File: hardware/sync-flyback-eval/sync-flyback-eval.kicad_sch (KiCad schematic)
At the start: 89 parts, among them J1 RJ45_LED_Shielded, Q1 SiR422DP, Q2 Si7898DP, Q3 MMDT3906, T1 PoE_Transformer, T2 Pulse_Transformer, U1 TPS23754PWPR, U2 TCMT1107

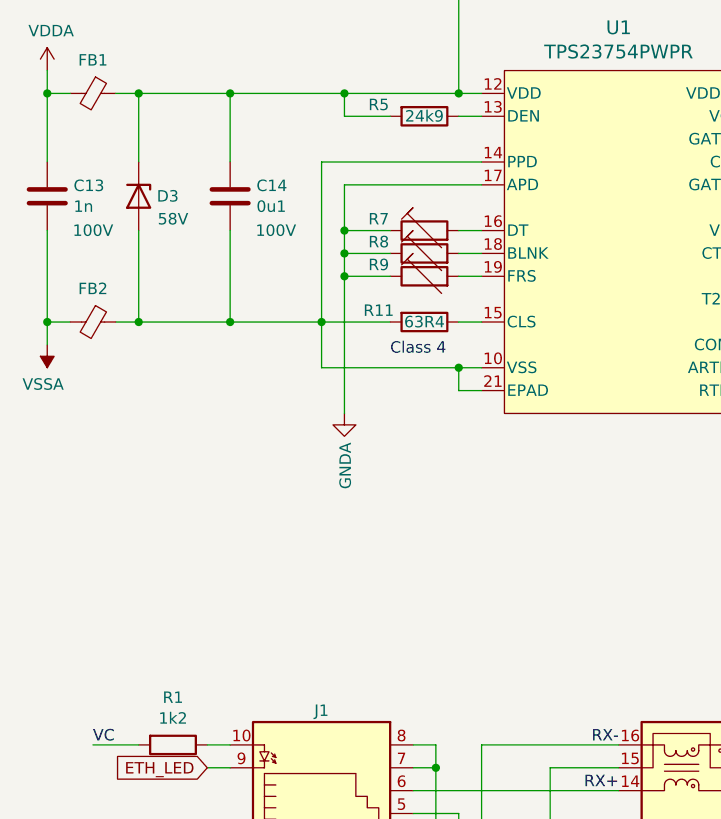
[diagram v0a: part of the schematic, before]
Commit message: flyback: use trimpots instead of trimmable resistors
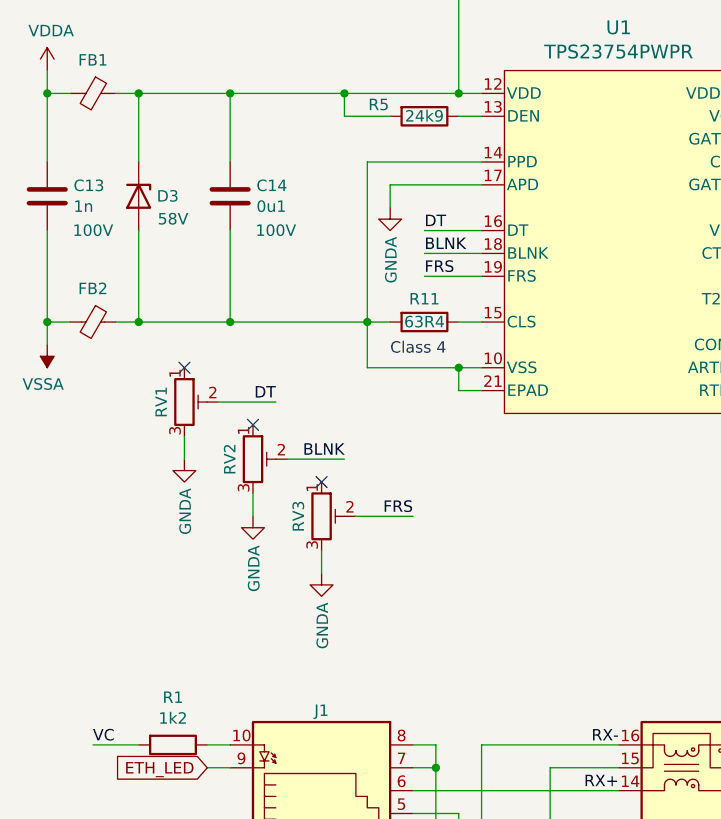
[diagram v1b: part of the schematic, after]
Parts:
- removed R7, R8, R9: 0-200k, symbol Device:R_Trim
- added RV1, RV2, RV3: 0-200k, symbol Device:R_Potentiometer_Trim
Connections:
- net GNDA: now also RV1.3, RV2.3, RV3.3
- net DT: now reaches U1.16 (DT)
- net DT: now also RV1.2
- net BLNK: now reaches U1.18 (BLNK)
- net BLNK: now also RV2.2
- net FRS: now reaches U1.19 (FRS)
- net FRS: now also RV3.2
- no-connect marks 0 -> 3

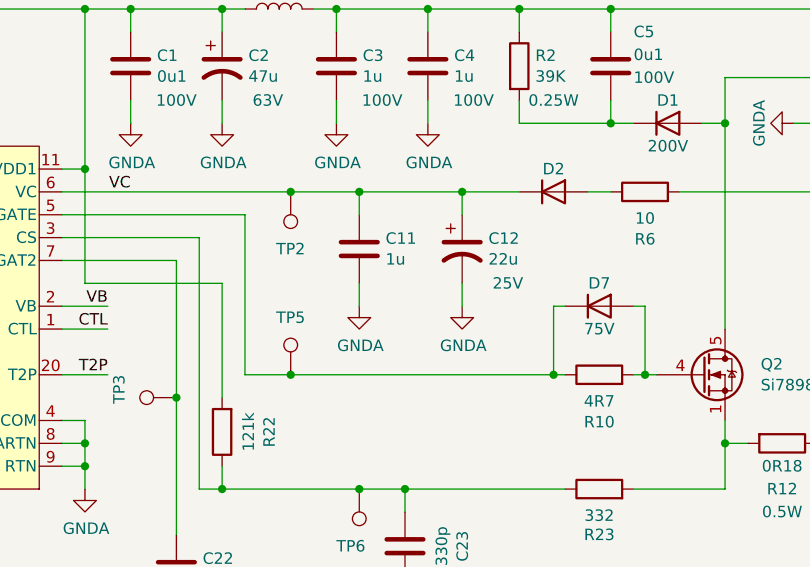
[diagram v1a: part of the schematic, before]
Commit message: flyback: add minimum-voltage specifier to C11
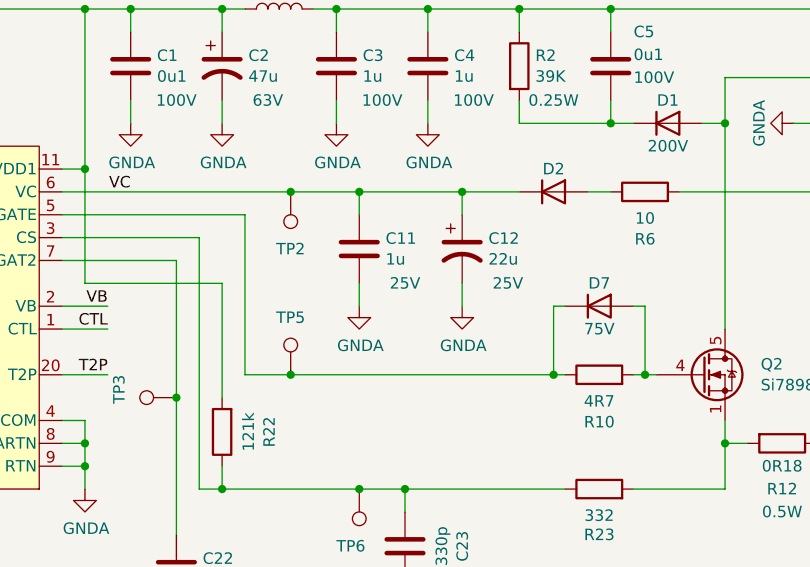
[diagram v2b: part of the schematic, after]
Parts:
- C11: Voltage (none) -> 25V
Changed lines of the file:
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@@
       (effects (font (size 1.27 1.27)) hide)
     )
+    (property "Voltage" "25V" (id 4) (at 132.08 54.61 0))
     (pin "1")
     (pin "2")

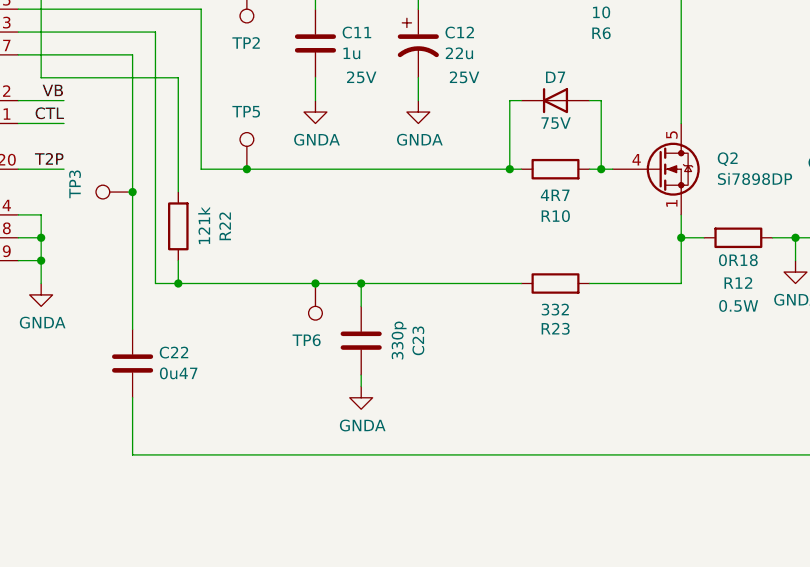
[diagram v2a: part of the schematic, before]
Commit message: flyback: use internal slope compensation by default
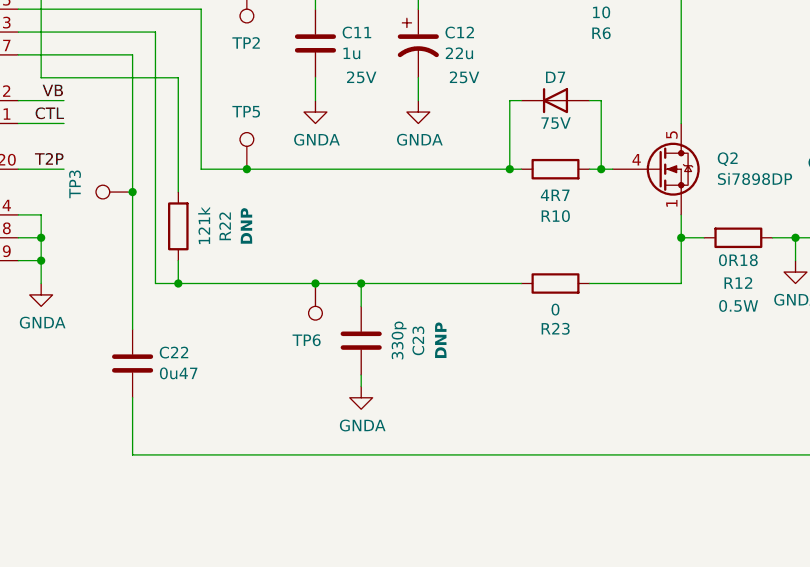
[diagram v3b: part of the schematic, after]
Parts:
- C23, R22: Placement (none) -> DNP
- R23: value 332 -> 0
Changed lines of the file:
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@@
   )
   (wire (pts (xy 106.68 96.52) (xy 182.88 96.52))
-    (stroke (width 0) (type default) (color 0 0 0 0))
+    (stroke (width 0) (type solid) (color 0 0 0 0))
   )
   (wire (pts (xy 236.22 140.97) (xy 236.22 143.51))
@@
       (effects (font (size 1.27 1.27)) hide)
     )
+    (property "Placement" "DNP" (id 4) (at 140.97 83.82 90)
+      (effects (font (size 1.27 1.27) bold))
+    )
     (pin "1")
     (pin "2")
@@
       (effects (font (size 1.27 1.27)) hide)
     )
+    (property "Placement" "DNP" (id 4) (at 119.38 71.12 90)
+      (effects (font (size 1.27 1.27) bold))
+    )
     (pin "1")
     (pin "2")
@@
     (in_bom yes) (on_board yes)
     (property "Reference" "R23" (id 0) (at 153.67 82.55 90))
-    (property "Value" "332" (id 1) (at 153.67 80.4164 90))
+    (property "Value" "0" (id 1) (at 153.67 80.4164 90))
     (property "Footprint" "Resistor_SMD:R_0402_1005Metric" (id 2) (at 153.67 79.248 90)
       (effects (font (size 1.27 1.27)) hide)
@@
     )
     (path "/f242d58c-dea3-4a02-8244-cad92f11809b"
-      (reference "R23") (unit 1) (value "332") (footprint "Resistor_SMD:R_0402_1005Metric")
+      (reference "R23") (unit 1) (value "0") (footprint "Resistor_SMD:R_0402_1005Metric")
     )
     (path "/9be08108-6f37-4bd8-8e20-fd0623e08fad"

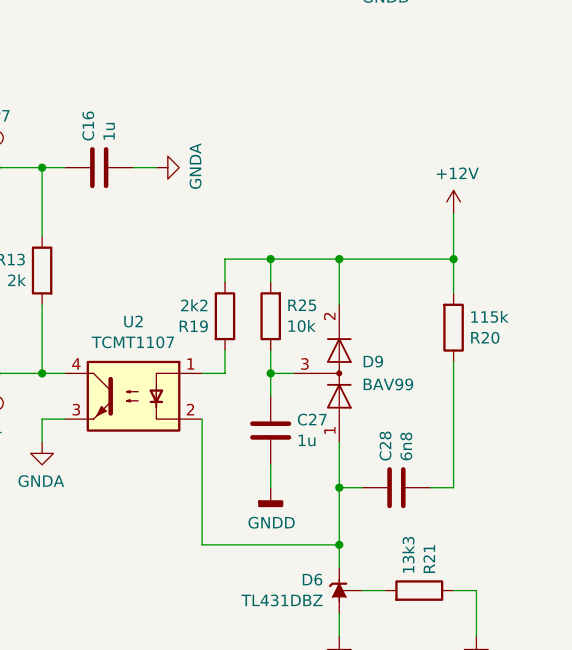
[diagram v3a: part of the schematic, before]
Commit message: flyback: use trimpot to make output voltage adjustable
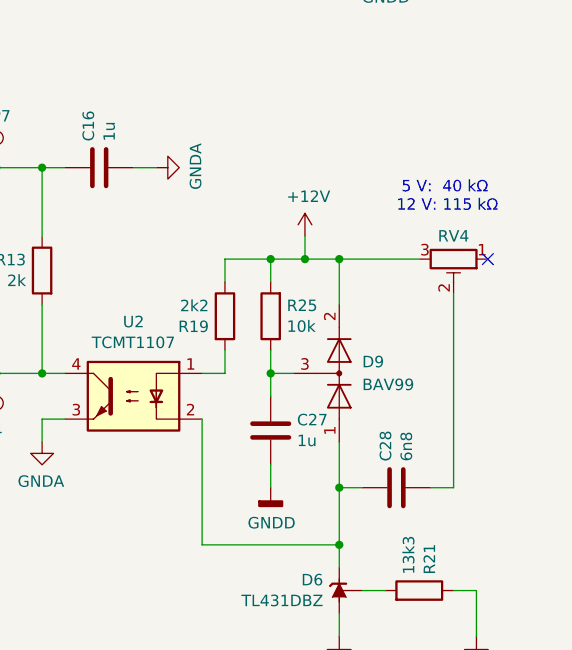
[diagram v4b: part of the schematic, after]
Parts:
- removed R20: 115k, Resistor_SMD:R_0402_1005Metric, symbol Device:R
- added RV4: 0-200k, symbol Device:R_Potentiometer_Trim
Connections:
- net +12V: now also RV4.3
- net at C28.2: now also RV4.2
- no-connect marks 3 -> 4
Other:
- note added: "5 V: 40 kΩ 12 V: 115 kΩ"
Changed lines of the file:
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@@
   (junction (at 236.22 39.37) (diameter 0) (color 0 0 0 0)
   )
-  (junction (at 256.54 118.11) (diameter 0) (color 0 0 0 0)
-  )
   (junction (at 243.84 143.51) (diameter 0) (color 0 0 0 0)
   )
@@
   (junction (at 58.42 116.84) (diameter 0) (color 0 0 0 0)
   )
+  (junction (at 240.03 118.11) (diameter 0) (color 0 0 0 0)
+  )
   (junction (at 243.84 149.86) (diameter 0) (color 0 0 0 0)
   )
@@
   (no_connect (at 45.72 85.09))
   (no_connect (at 38.1 78.74))
+  (no_connect (at 260.35 118.11))
   (wire (pts (xy 30.48 80.01) (xy 30.48 82.55))
     (stroke (width 0) (type default) (color 0 0 0 0))
@@
     (stroke (width 0) (type default) (color 0 0 0 0))
   )
-  (wire (pts (xy 256.54 118.11) (xy 256.54 113.03))
-    (stroke (width 0) (type default) (color 0 0 0 0))
-  )
   (wire (pts (xy 20.32 175.26) (xy 33.02 175.26))
     (stroke (width 0) (type default) (color 0 0 0 0))
@@
     (stroke (width 0) (type default) (color 0 0 0 0))
   )
+  (wire (pts (xy 240.03 118.11) (xy 243.84 118.11))
+    (stroke (width 0) (type default) (color 0 0 0 0))
+  )
   (wire (pts (xy 48.26 41.91) (xy 35.56 41.91))
     (stroke (width 0) (type default) (color 0 0 0 0))
@@
     (stroke (width 0) (type default) (color 0 0 0 0))
   )
-  (wire (pts (xy 256.54 118.11) (xy 256.54 121.92))
+  (wire (pts (xy 96.52 54.61) (xy 111.76 54.61))
     (stroke (width 0) (type default) (color 0 0 0 0))
   )
-  (wire (pts (xy 96.52 54.61) (xy 111.76 54.61))
+  (wire (pts (xy 256.54 121.92) (xy 256.54 143.51))
     (stroke (width 0) (type default) (color 0 0 0 0))
   )
@@
     (stroke (width 0) (type default) (color 0 0 0 0))
   )
-  (wire (pts (xy 256.54 129.54) (xy 256.54 143.51))
-    (stroke (width 0) (type default) (color 0 0 0 0))
-  )
   (wire (pts (xy 63.5 114.3) (xy 78.74 114.3))
     (stroke (width 0) (type default) (color 0 0 0 0))
@@
     (stroke (width 0) (type default) (color 0 0 0 0))
   )
-  (wire (pts (xy 236.22 118.11) (xy 243.84 118.11))
+  (wire (pts (xy 243.84 118.11) (xy 252.73 118.11))
+    (stroke (width 0) (type default) (color 0 0 0 0))
+  )
+  (wire (pts (xy 236.22 118.11) (xy 240.03 118.11))
     (stroke (width 0) (type default) (color 0 0 0 0))
   )
@@
     (stroke (width 0) (type default) (color 0 0 0 0))
   )
-  (wire (pts (xy 243.84 118.11) (xy 256.54 118.11))
-    (stroke (width 0) (type default) (color 0 0 0 0))
-  )
   (wire (pts (xy 200.66 107.95) (xy 205.74 107.95))
     (stroke (width 0) (type default) (color 0 0 0 0))
@@
     (stroke (width 0) (type default) (color 0 0 0 0))
   )
+  (wire (pts (xy 240.03 115.57) (xy 240.03 118.11))
+    (stroke (width 0) (type default) (color 0 0 0 0))
+  )
   (wire (pts (xy 15.24 41.91) (xy 15.24 39.37))
     (stroke (width 0) (type default) (color 0 0 0 0))
@@
     (stroke (width 0) (type default) (color 0 0 0 0))
   )
+  (text " 5 V:  40 kΩ\n12 V: 115 kΩ" (at 250.19 113.03 0)
+    (effects (font (size 1.27 1.27)) (justify left bottom))
+  )
   (text "Classification Resistor\n\nClass 0 (0.44 W-13W) - 1270 Ohm\nClass 1 (0.44 W-3.84 W) - 243 Ohm\nClass 2 (3.84 W-6.49 W) - 137 Ohm\nClass 3 (6.49 W-13 W) - 90.9 Ohm\nClass 4 (13 W-25.5 W) - 63.4 Ohm"
     (at 13.97 29.21 0)
@@
     (pin "3")
   )
-  (symbol (lib_id "Device:R") (at 256.54 125.73 0) (mirror x) (unit 1)
-    (in_bom yes) (on_board yes)
-    (property "Reference" "R20" (id 0) (at 258.318 126.8984 0)
-      (effects (font (size 1.27 1.27)) (justify left))
-    )
-    (property "Value" "115k" (id 1) (at 258.318 124.587 0)
-      (effects (font (size 1.27 1.27)) (justify left))
-    )
-    (property "Footprint" "Resistor_SMD:R_0402_1005Metric" (id 2) (at 254.762 125.73 90)
-      (effects (font (size 1.27 1.27)) hide)
-    )
-    (property "Datasheet" "~" (id 3) (at 256.54 125.73 0)
-      (effects (font (size 1.27 1.27)) hide)
-    )
-    (pin "1")
-    (pin "2")
-  )
   (symbol (lib_id "Device:R") (at 252.73 154.94 270) (mirror x) (unit 1)
     (in_bom yes) (on_board yes)
@@
     (pin "1")
   )
-  (symbol (lib_id "power:+12V") (at 256.54 113.03 0) (unit 1)
+  (symbol (lib_id "power:+12V") (at 240.03 115.57 0) (unit 1)
     (in_bom yes) (on_board yes)
-    (property "Reference" "#PWR024" (id 0) (at 256.54 116.84 0)
+    (property "Reference" "#PWR024" (id 0) (at 240.03 119.38 0)
       (effects (font (size 1.27 1.27)) hide)
     )
-    (property "Value" "+12V" (id 1) (at 256.921 108.6358 0))
-    (property "Footprint" "" (id 2) (at 256.54 113.03 0)
+    (property "Value" "+12V" (id 1) (at 240.411 111.1758 0))
+    (property "Footprint" "" (id 2) (at 240.03 115.57 0)
       (effects (font (size 1.27 1.27)) hide)
     )
-    (property "Datasheet" "" (id 3) (at 256.54 113.03 0)
+    (property "Datasheet" "" (id 3) (at 240.03 115.57 0)
       (effects (font (size 1.27 1.27)) hide)
     )
@@
     (pin "1")
   )
+  (symbol (lib_id "Device:R_Potentiometer_Trim") (at 256.54 118.11 270) (unit 1)
+    (in_bom yes) (on_board yes)
+    (property "Reference" "RV4" (id 0) (at 256.54 115.57 90))
+    (property "Value" "0-200k" (id 1) (at 256.54 111.76 90)
+      (effects (font (size 1.27 1.27)) hide)
+    )
+    (property "Footprint" "" (id 2) (at 256.54 118.11 0)
+      (effects (font (size 1.27 1.27)) hide)
+    )
+    (property "Datasheet" "~" (id 3) (at 256.54 118.11 0)
+      (effects (font (size 1.27 1.27)) hide)
+    )
+    (pin "1")
+    (pin "2")
+    (pin "3")
+  )
   (symbol (lib_id "Device:R") (at 111.76 71.12 180) (unit 1)
     (in_bom yes) (on_board yes)
@@
       (reference "R19") (unit 1) (value "2k2") (footprint "Resistor_SMD:R_0402_1005Metric")
     )
-    (path "/00000000-0000-0000-0000-00005ddb94b5"
-      (reference "R20") (unit 1) (value "115k") (footprint "Resistor_SMD:R_0402_1005Metric")
-    )
     (path "/00000000-0000-0000-0000-00005ddb986a"
       (reference "R21") (unit 1) (value "13k3") (footprint "Resistor_SMD:R_0402_1005Metric")
@@
       (reference "RV3") (unit 1) (value "0-200k") (footprint "")
     )
+    (path "/981d4e4a-c5d7-441c-8be5-cfd05c87b9e8"
+      (reference "RV4") (unit 1) (value "0-200k") (footprint "")
+    )
     (path "/00000000-0000-0000-0000-00005dad1b8a"
